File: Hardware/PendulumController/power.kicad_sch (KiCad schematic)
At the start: 8 parts, among them J301 19V Input, U301 NCV1117ST50T3G

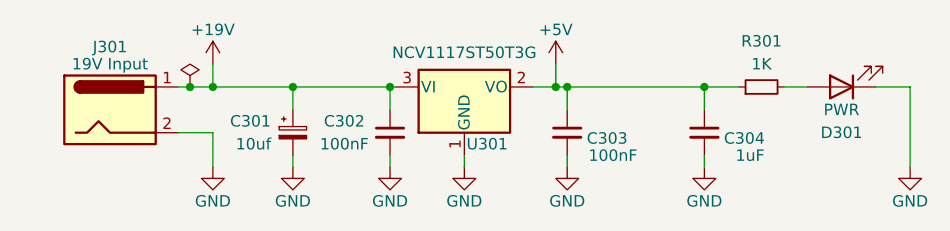
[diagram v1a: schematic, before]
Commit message: Configure kibot config
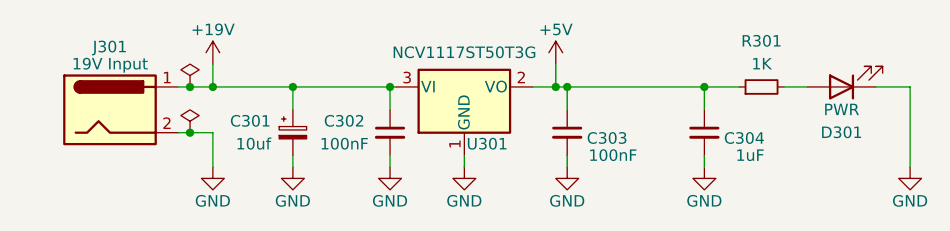
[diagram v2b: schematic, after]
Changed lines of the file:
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@@
     (comment 4 "Release: ${FULL_REVISION}")
   )
+  (junction (at 114.3 88.265) (diameter 0) (color 0 0 0 0)
+  )
   (junction (at 171.45 88.265) (diameter 0) (color 0 0 0 0)
   )
-  (junction (at 114.3 88.265) (diameter 0) (color 0 0 0 0)
+  (junction (at 114.3 93.345) (diameter 0) (color 0 0 0 0)
   )
   (junction (at 156.21 88.265) (diameter 0) (color 0 0 0 0)
@@
     (stroke (width 0) (type default) (color 0 0 0 0))
   )
+  (wire (pts (xy 171.45 97.155) (xy 171.45 95.885))
+    (stroke (width 0) (type default) (color 0 0 0 0))
+  )
+  (wire (pts (xy 156.21 88.265) (xy 154.94 88.265))
+    (stroke (width 0) (type default) (color 0 0 0 0))
+  )
+  (wire (pts (xy 156.21 88.265) (xy 171.45 88.265))
+    (stroke (width 0) (type default) (color 0 0 0 0))
+  )
   (wire (pts (xy 116.84 88.265) (xy 125.73 88.265))
     (stroke (width 0) (type default) (color 0 0 0 0))
   )
-  (wire (pts (xy 171.45 97.155) (xy 171.45 95.885))
-    (stroke (width 0) (type default) (color 0 0 0 0))
-  )
-  (wire (pts (xy 156.21 88.265) (xy 154.94 88.265))
-    (stroke (width 0) (type default) (color 0 0 0 0))
-  )
-  (wire (pts (xy 156.21 88.265) (xy 171.45 88.265))
-    (stroke (width 0) (type default) (color 0 0 0 0))
-  )
   (wire (pts (xy 190.5 88.265) (xy 194.31 88.265))
     (stroke (width 0) (type default) (color 0 0 0 0))
@@
     (stroke (width 0) (type default) (color 0 0 0 0))
   )
+  (wire (pts (xy 171.45 88.265) (xy 171.45 90.805))
+    (stroke (width 0) (type default) (color 0 0 0 0))
+  )
+  (wire (pts (xy 136.525 88.265) (xy 136.525 90.805))
+    (stroke (width 0) (type default) (color 0 0 0 0))
+  )
+  (wire (pts (xy 114.3 93.345) (xy 113.03 93.345))
+    (stroke (width 0) (type default) (color 0 0 0 0))
+  )
+  (wire (pts (xy 180.34 88.265) (xy 182.88 88.265))
+    (stroke (width 0) (type default) (color 0 0 0 0))
+  )
+  (wire (pts (xy 156.21 88.265) (xy 156.21 90.805))
+    (stroke (width 0) (type default) (color 0 0 0 0))
+  )
   (wire (pts (xy 114.3 88.265) (xy 116.84 88.265))
     (stroke (width 0) (type default) (color 0 0 0 0))
   )
-  (wire (pts (xy 171.45 88.265) (xy 171.45 90.805))
-    (stroke (width 0) (type default) (color 0 0 0 0))
-  )
-  (wire (pts (xy 136.525 88.265) (xy 136.525 90.805))
-    (stroke (width 0) (type default) (color 0 0 0 0))
-  )
-  (wire (pts (xy 180.34 88.265) (xy 182.88 88.265))
-    (stroke (width 0) (type default) (color 0 0 0 0))
-  )
-  (wire (pts (xy 156.21 88.265) (xy 156.21 90.805))
-    (stroke (width 0) (type default) (color 0 0 0 0))
-  )
-  (wire (pts (xy 116.84 93.345) (xy 113.03 93.345))
+  (wire (pts (xy 116.84 93.345) (xy 114.3 93.345))
     (stroke (width 0) (type default) (color 0 0 0 0))
   )
@@
     (pin "2")
   )
+  (symbol (lib_id "power:PWR_FLAG") (at 114.3 88.265 0) (unit 1)
+    (in_bom yes) (on_board yes) (fields_autoplaced)
+    (property "Reference" "#FLG?" (id 0) (at 114.3 86.36 0)
+      (effects (font (size 1.27 1.27)) hide)
+    )
+    (property "Value" "PWR_FLAG" (id 1) (at 114.3 82.55 0)
+      (effects (font (size 1.27 1.27)) hide)
+    )
+    (property "Footprint" "" (id 2) (at 114.3 88.265 0)
+      (effects (font (size 1.27 1.27)) hide)
+    )
+    (property "Datasheet" "~" (id 3) (at 114.3 88.265 0)
+      (effects (font (size 1.27 1.27)) hide)
+    )
+    (pin "1")
+  )
   (symbol (lib_id "power:GND") (at 125.73 97.155 0) (unit 1)
     (in_bom yes) (on_board yes)
@@
     (pin "1")
   )
-  (symbol (lib_id "power:PWR_FLAG") (at 114.3 88.265 0) (unit 1)
+  (symbol (lib_id "power:PWR_FLAG") (at 114.3 93.345 0) (unit 1)
     (in_bom yes) (on_board yes) (fields_autoplaced)
-    (property "Reference" "#FLG0101" (id 0) (at 114.3 86.36 0)
-      (effects (font (size 1.27 1.27)) hide)
-    )
-    (property "Value" "PWR_FLAG" (id 1) (at 114.3 82.55 0)
-      (effects (font (size 1.27 1.27)) hide)
-    )
-    (property "Footprint" "" (id 2) (at 114.3 88.265 0)
-      (effects (font (size 1.27 1.27)) hide)
-    )
-    (property "Datasheet" "~" (id 3) (at 114.3 88.265 0)
-      (effects (font (size 1.27 1.27)) hide)
-    )
+    (property "Reference" "#FLG?" (id 0) (at 114.3 91.44 0)
+      (effects (font (size 1.27 1.27)) hide)
+    )
+    (property "Value" "PWR_FLAG" (id 1) (at 114.3 87.63 0)
+      (effects (font (size 1.27 1.27)) hide)
+    )
+    (property "Footprint" "" (id 2) (at 114.3 93.345 0)
+      (effects (font (size 1.27 1.27)) hide)
+    )
+    (property "Datasheet" "~" (id 3) (at 114.3 93.345 0)
+      (effects (font (size 1.27 1.27)) hide)
+    )

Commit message: Cleanup readme and fix ERC
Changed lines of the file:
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@@
   (junction (at 171.45 88.265) (diameter 0) (color 0 0 0 0)
   )
-  (junction (at 114.3 93.345) (diameter 0) (color 0 0 0 0)
-  )
   (junction (at 156.21 88.265) (diameter 0) (color 0 0 0 0)
   )
@@
     (stroke (width 0) (type default) (color 0 0 0 0))
   )
-  (wire (pts (xy 114.3 93.345) (xy 113.03 93.345))
-    (stroke (width 0) (type default) (color 0 0 0 0))
-  )
   (wire (pts (xy 180.34 88.265) (xy 182.88 88.265))
     (stroke (width 0) (type default) (color 0 0 0 0))
@@
     (stroke (width 0) (type default) (color 0 0 0 0))
   )
-  (wire (pts (xy 116.84 93.345) (xy 114.3 93.345))
+  (wire (pts (xy 113.03 93.345) (xy 116.84 93.345))
     (stroke (width 0) (type default) (color 0 0 0 0))
   )
@@
       (effects (font (size 1.27 1.27)) hide)
     )
-    (pin "1")
-  )
-  (symbol (lib_id "power:PWR_FLAG") (at 114.3 93.345 0) (unit 1)
-    (in_bom yes) (on_board yes) (fields_autoplaced)
-    (property "Reference" "#FLG?" (id 0) (at 114.3 91.44 0)
-      (effects (font (size 1.27 1.27)) hide)
-    )
-    (property "Value" "PWR_FLAG" (id 1) (at 114.3 87.63 0)
-      (effects (font (size 1.27 1.27)) hide)
-    )
-    (property "Footprint" "" (id 2) (at 114.3 93.345 0)
-      (effects (font (size 1.27 1.27)) hide)
-    )
-    (property "Datasheet" "~" (id 3) (at 114.3 93.345 0)
-      (effects (font (size 1.27 1.27)) hide)
-    )

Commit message: V1 Board (#3)
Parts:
- removed J301: 19V Input, Connector_BarrelJack:BarrelJack_GCT_DCJ200-10-A_Horizontal, symbol Connector:Barrel_Jack
- added J302: 19V Input, TerminalBlock_Phoenix:TerminalBlock_Phoenix_MKDS-3-2-5.08_1x02_P5.08mm_Horizontal, symbol Connector:Screw_Terminal_01x02
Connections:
- net +19V: now also J302.2 (Pin_2)
- net GND: now also J302.1 (Pin_1)
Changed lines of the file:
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@@
     (stroke (width 0) (type default) (color 0 0 0 0))
   )
-  (wire (pts (xy 113.03 93.345) (xy 116.84 93.345))
-    (stroke (width 0) (type default) (color 0 0 0 0))
-  )
-  (wire (pts (xy 116.84 97.155) (xy 116.84 93.345))
+  (wire (pts (xy 113.03 90.805) (xy 116.84 90.805))
+    (stroke (width 0) (type default) (color 0 0 0 0))
+  )
+  (wire (pts (xy 116.84 97.155) (xy 116.84 90.805))
     (stroke (width 0) (type default) (color 0 0 0 0))
   )
@@
     (stroke (width 0) (type default) (color 0 0 0 0))
   )
-  (symbol (lib_id "Connector:Barrel_Jack") (at 105.41 90.805 0) (unit 1)
-    (in_bom yes) (on_board yes)
-    (property "Reference" "J301" (id 0) (at 105.41 83.82 0))
-    (property "Value" "19V Input" (id 1) (at 105.41 85.725 0))
-    (property "Footprint" "Connector_BarrelJack:BarrelJack_GCT_DCJ200-10-A_Horizontal" (id 2) (at 106.68 91.821 0)
-      (effects (font (size 1.27 1.27)) hide)
-    )
-    (property "Datasheet" "~" (id 3) (at 106.68 91.821 0)
-      (effects (font (size 1.27 1.27)) hide)
-    )
-    (pin "1")
-    (pin "2")
-  )
-  (symbol (lib_id "power:GND") (at 144.78 97.155 0) (unit 1)
+  (symbol (lib_id "Connector:Screw_Terminal_01x02") (at 107.95 90.805 180) (unit 1)
+    (in_bom yes) (on_board yes)
+    (property "Reference" "J302" (id 0) (at 100.965 88.265 0))
+    (property "Value" "19V Input" (id 1) (at 100.965 90.805 0))
+    (property "Footprint" "TerminalBlock_Phoenix:TerminalBlock_Phoenix_MKDS-3-2-5.08_1x02_P5.08mm_Horizontal" (id 2) (at 107.95 90.805 0)
+      (effects (font (size 1.27 1.27)) hide)
+    )
+    (property "Datasheet" "~" (id 3) (at 107.95 90.805 0)
+      (effects (font (size 1.27 1.27)) hide)
+    )
+    (pin "1")
+    (pin "2")
+  )
+  (symbol (lib_name "GND_1") (lib_id "power:GND") (at 144.78 97.155 0) (unit 1)
     (in_bom yes) (on_board yes)
     (property "Reference" "#PWR0110" (id 0) (at 144.78 103.505 0)
@@
     (pin "2")
   )
-  (symbol (lib_id "power:GND") (at 156.21 97.155 0) (unit 1)
+  (symbol (lib_name "GND_5") (lib_id "power:GND") (at 156.21 97.155 0) (unit 1)
     (in_bom yes) (on_board yes)
     (property "Reference" "#PWR0113" (id 0) (at 156.21 103.505 0)
@@
     (pin "1")
   )
-  (symbol (lib_id "power:GND") (at 136.525 97.155 0) (unit 1)
+  (symbol (lib_name "GND_3") (lib_id "power:GND") (at 136.525 97.155 0) (unit 1)
     (in_bom yes) (on_board yes)
     (property "Reference" "#PWR0111" (id 0) (at 136.525 103.505 0)
@@
     (pin "2")
   )
-  (symbol (lib_id "power:GND") (at 116.84 97.155 0) (unit 1)
+  (symbol (lib_name "GND_2") (lib_id "power:GND") (at 116.84 97.155 0) (unit 1)
     (in_bom yes) (on_board yes)
     (property "Reference" "#PWR0108" (id 0) (at 116.84 103.505 0)
@@
     (pin "1")
   )
-  (symbol (lib_id "power:GND") (at 125.73 97.155 0) (unit 1)
+  (symbol (lib_name "GND_4") (lib_id "power:GND") (at 125.73 97.155 0) (unit 1)
     (in_bom yes) (on_board yes)
     (property "Reference" "#PWR0107" (id 0) (at 125.73 103.505 0)
@@
     (pin "1")
   )
-  (symbol (lib_id "power:GND") (at 171.45 97.155 0) (unit 1)
+  (symbol (lib_name "GND_6") (lib_id "power:GND") (at 171.45 97.155 0) (unit 1)
     (in_bom yes) (on_board yes)
     (property "Reference" "#PWR0112" (id 0) (at 171.45 103.505 0)
